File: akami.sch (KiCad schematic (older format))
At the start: 66 parts, among them J1 USB_C_Receptacle_USB2.0, J2 Conn_01x01, J3 Conn_01x01, Q1 DMP21D0UT, Q2 DMP21D0UT, Q3 DMP21D0UT, U1 nRF52840, U2 TP4054, U3 LP5912-3.3DRV, U4 ProMicro_2, Y1 32MHz, Y2 32.768 kHz

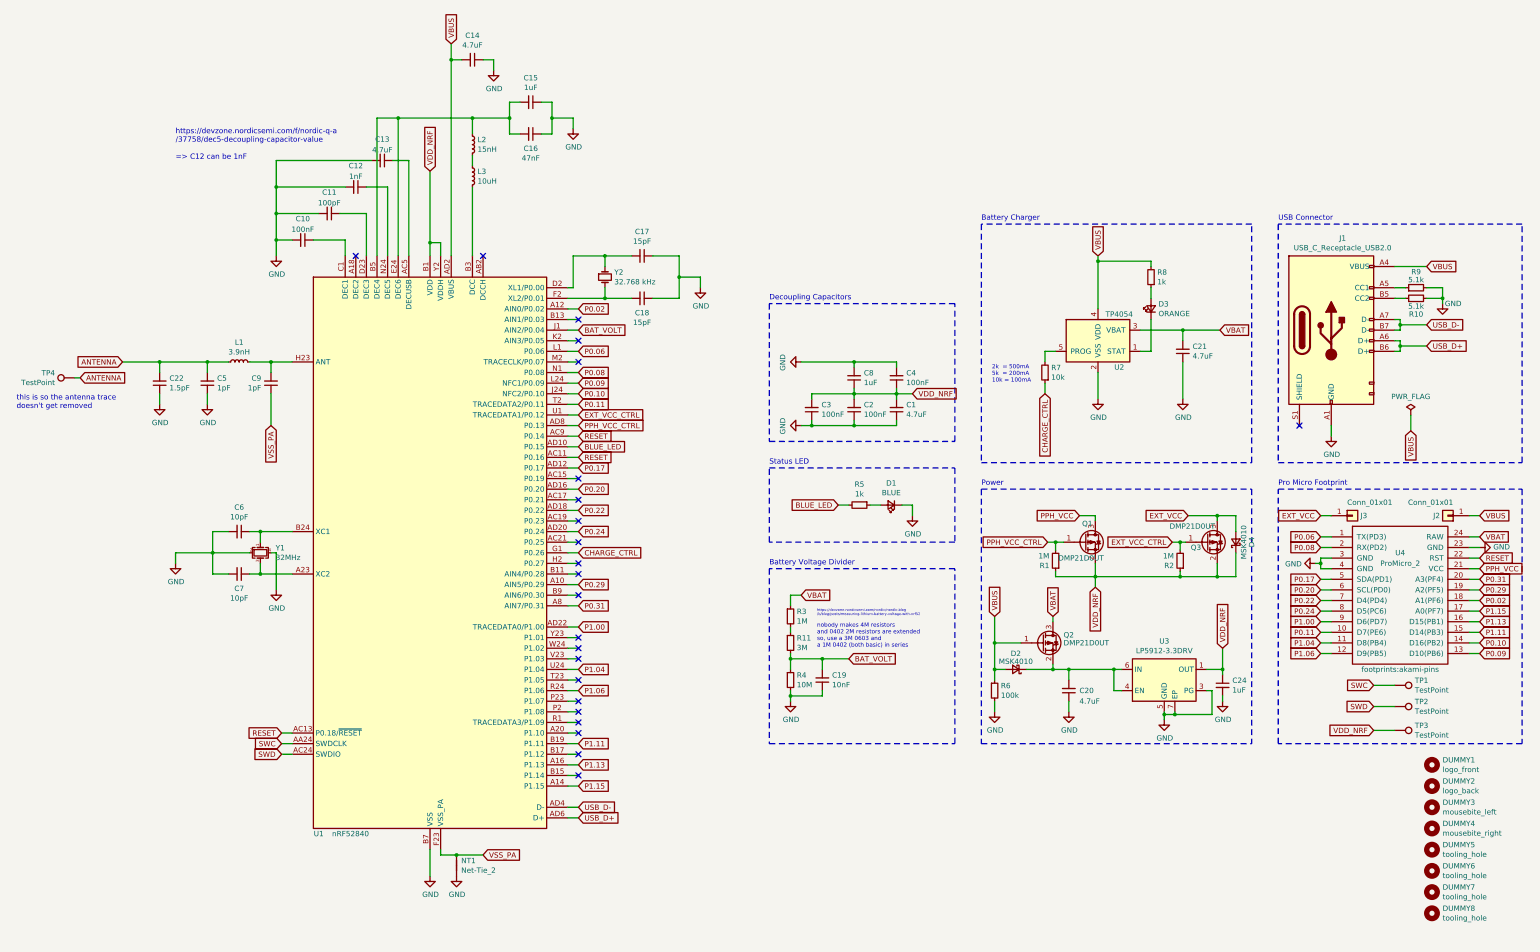
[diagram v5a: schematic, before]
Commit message: rev 3.2
1. re-layout and re-route the entire thing
2. as part of (1), move the nrf chip up by 0.75mm
3. add a 1uF capacitor on the VBUS input to the charger IC
4. move components further away from the USB connector since that
   has to be hand-soldered
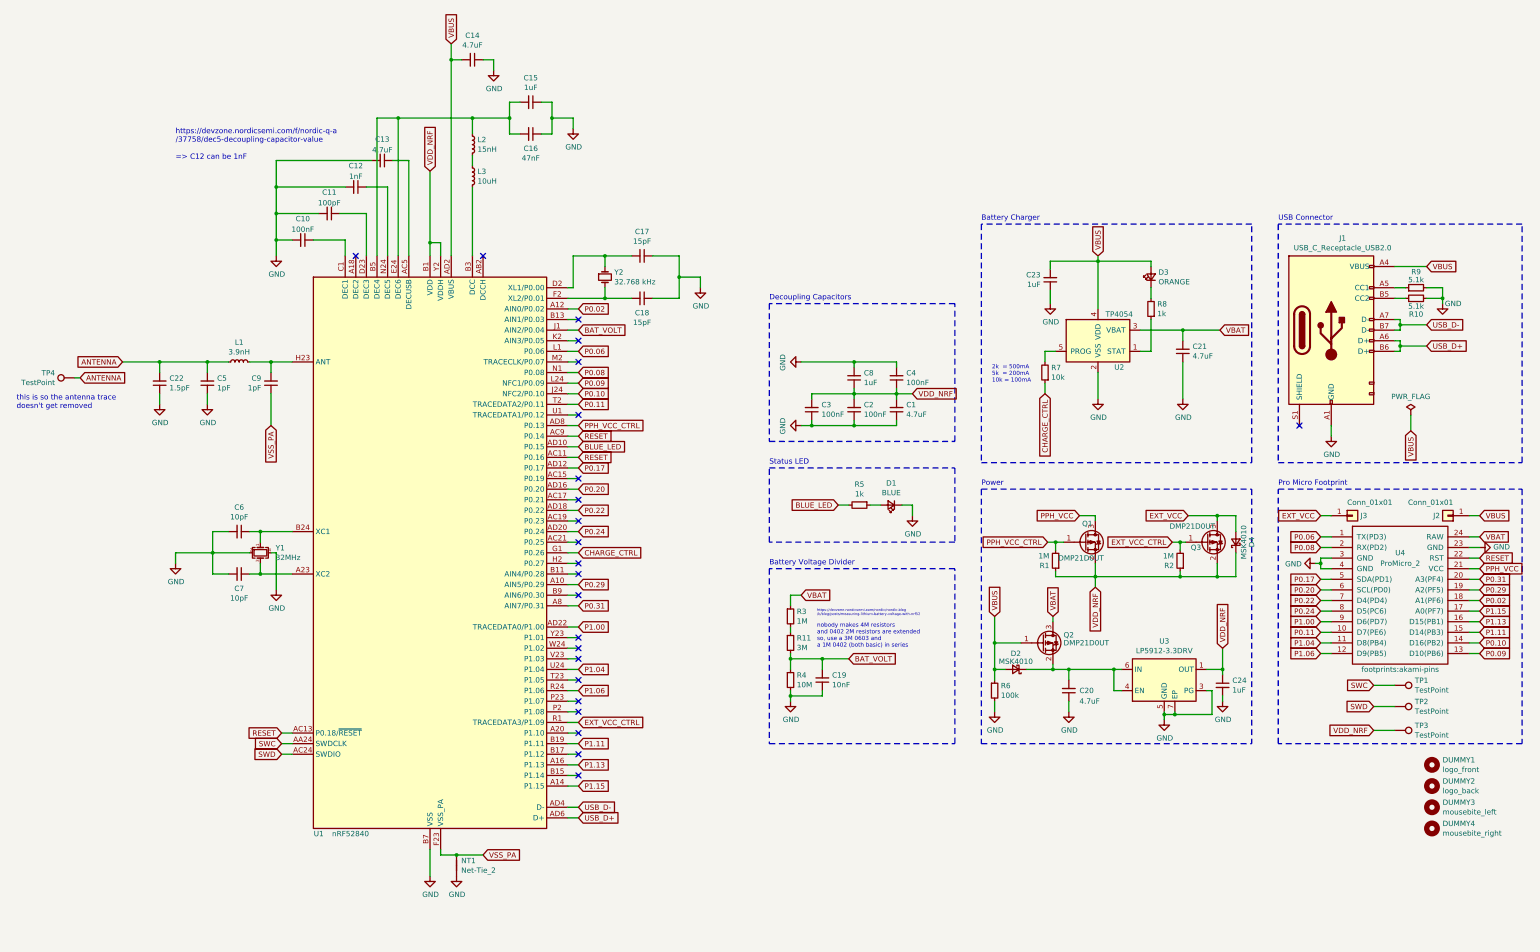
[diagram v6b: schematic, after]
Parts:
- removed DUMMY5, DUMMY6, DUMMY7, DUMMY8: tooling_hole, footprints:jlcpcb_tooling_hole, symbol Mechanical:MountingHole
- added C23: 1uF, Capacitor_SMD:C_0402_1005Metric, symbol Device:C_Small
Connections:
- net EXT_VCC_CTRL: now also U1.R1 (TRACEDATA3/P1.09); no longer U1.U1 (TRACEDATA1/P0.12)
- net GND: now also C23.1
- net VBUS: now also D3.2 (A), C23.2; no longer R8.2
- net at U2.1 (STAT): now also R8.1; no longer D3.1 (K)
- new net: D3.1 (K), R8.2
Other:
- moved on the sheet: D3, R8
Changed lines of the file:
@@
-$EndComp
-$Comp
-L Device:C_Small C8
-U 1 1 5FEB5801
-P 9200 4300
-F 0 "C8" H 9108 4254 50  0000 R CNN
-F 1 "1uF" H 9108 4345 50  0000 R CNN
-F 2 "Capacitor_SMD:C_0402_1005Metric" H 9200 4300 50  0001 C CNN
-F 3 "~" H 9200 4300 50  0001 C CNN
-F 4 "C52923" H 9200 4300 50  0001 C CNN "LCSC Part"
-	1    9200 4300
-	-1   0    0    1
 $EndComp
 $Comp
@@
 L Device:LED_Small D3
 U 1 1 5FFAD26F
-P 12000 3650
-F 0 "D3" V 12046 3580 50  0000 R CNN
-F 1 "ORANGE" V 11955 3580 50  0000 R CNN
-F 2 "LED_SMD:LED_0603_1608Metric" V 12000 3650 50  0001 C CNN
-F 3 "~" V 12000 3650 50  0001 C CNN
-F 4 "C2286" H 12000 3650 50  0001 C CNN "LCSC Part"
-	1    12000 3650
+P 12000 3350
+F 0 "D3" V 12046 3280 50  0000 R CNN
+F 1 "ORANGE" V 11955 3280 50  0000 R CNN
+F 2 "LED_SMD:LED_0603_1608Metric" V 12000 3350 50  0001 C CNN
+F 3 "~" V 12000 3350 50  0001 C CNN
+F 4 "C2286" H 12000 3350 50  0001 C CNN "LCSC Part"
+	1    12000 3350
 	0    -1   -1   0
 $EndComp
@@
 L Device:R_Small R8
 U 1 1 5FFBCDAA
-P 12000 3350
-F 0 "R8" H 11941 3304 50  0000 R CNN
-F 1 "1k" H 11941 3395 50  0000 R CNN
-F 2 "Resistor_SMD:R_0402_1005Metric" H 12000 3350 50  0001 C CNN
-F 3 "~" H 12000 3350 50  0001 C CNN
-F 4 "C11702" H 12000 3350 50  0001 C CNN "LCSC Part"
-	1    12000 3350
+P 12000 3650
+F 0 "R8" H 11941 3604 50  0000 R CNN
+F 1 "1k" H 11941 3695 50  0000 R CNN
+F 2 "Resistor_SMD:R_0402_1005Metric" H 12000 3650 50  0001 C CNN
+F 3 "~" H 12000 3650 50  0001 C CNN
+F 4 "C11702" H 12000 3650 50  0001 C CNN "LCSC Part"
+	1    12000 3650
 	-1   0    0    1
 $EndComp
@@
 NoConn ~ 6600 7350
 NoConn ~ 6600 7450
-NoConn ~ 6600 7550
 NoConn ~ 6600 7850
 NoConn ~ 6600 8050
@@
 $EndComp
 $Comp
-L Mechanical:MountingHole DUMMY5
-U 1 1 60BBBC37
-P 14650 8750
-F 0 "DUMMY5" H 14750 8796 50  0000 L CNN
-F 1 "tooling_hole" H 14750 8705 50  0000 L CNN
-F 2 "footprints:jlcpcb_tooling_hole" H 14650 8750 50  0001 C CNN
-F 3 "~" H 14650 8750 50  0001 C CNN
-	1    14650 8750
-	1    0    0    -1
-$EndComp
-$Comp
-L Mechanical:MountingHole DUMMY6
-U 1 1 60BBDE3A
-P 14650 8950
-F 0 "DUMMY6" H 14750 8996 50  0000 L CNN
-F 1 "tooling_hole" H 14750 8905 50  0000 L CNN
-F 2 "footprints:jlcpcb_tooling_hole" H 14650 8950 50  0001 C CNN
-F 3 "~" H 14650 8950 50  0001 C CNN
-	1    14650 8950
-	1    0    0    -1
-$EndComp
-$Comp
-L Mechanical:MountingHole DUMMY8
-U 1 1 60BBE1CE
-P 14650 9350
-F 0 "DUMMY8" H 14750 9396 50  0000 L CNN
-F 1 "tooling_hole" H 14750 9305 50  0000 L CNN
-F 2 "footprints:jlcpcb_tooling_hole" H 14650 9350 50  0001 C CNN
-F 3 "~" H 14650 9350 50  0001 C CNN
-	1    14650 9350
-	1    0    0    -1
-$EndComp
-$Comp
-L Mechanical:MountingHole DUMMY7
-U 1 1 60BBE5E3
-P 14650 9150
-F 0 "DUMMY7" H 14750 9196 50  0000 L CNN
-F 1 "tooling_hole" H 14750 9105 50  0000 L CNN
-F 2 "footprints:jlcpcb_tooling_hole" H 14650 9150 50  0001 C CNN
-F 3 "~" H 14650 9150 50  0001 C CNN
-	1    14650 9150
-	1    0    0    -1
-$EndComp
-$Comp
 L Connector_Generic:Conn_01x01 J3
 U 1 1 6009CB51
@@
 Wire Wire Line
 	6600 4650 6500 4650
-Text GLabel 6600 4650 2    50   Input ~ 0
+Text GLabel 6600 7550 2    50   Input ~ 0
 EXT_VCC_CTRL
 NoConn ~ 6600 7650
@@
 	1    0    0    -1
 $EndComp
+NoConn ~ 6600 4650
+$Comp
+L Device:C_Small C8
+U 1 1 5FEB5801
+P 9200 4300
+F 0 "C8" H 9108 4254 50  0000 R CNN
+F 1 "1uF" H 9108 4345 50  0000 R CNN
+F 2 "Capacitor_SMD:C_0402_1005Metric" H 9200 4300 50  0001 C CNN
+F 3 "~" H 9200 4300 50  0001 C CNN
+F 4 "C52923" H 9200 4300 50  0001 C CNN "LCSC Part"
+	1    9200 4300
+	-1   0    0    1
+$EndComp
+$Comp
+L Device:C_Small C23
+U 1 1 6025FBAA
+P 11050 3375
+F 0 "C23" H 11142 3329 50  0000 L CNN
+F 1 "1uF" H 11142 3420 50  0000 L CNN
+F 2 "Capacitor_SMD:C_0402_1005Metric" H 11050 3375 50  0001 C CNN
+F 3 "~" H 11050 3375 50  0001 C CNN
+F 4 "C52923" H 11050 3375 50  0001 C CNN "LCSC Part"
+	1    11050 3375
+	-1   0    0    1
+$EndComp
+$Comp
+L power:GND #PWR02
+U 1 1 60276B08
+P 11050 3600
+F 0 "#PWR02" H 11050 3350 50  0001 C CNN
+F 1 "GND" H 11055 3427 50  0000 C CNN
+F 2 "" H 11050 3600 50  0001 C CNN
+F 3 "" H 11050 3600 50  0001 C CNN
+	1    11050 3600
+	1    0    0    -1
+$EndComp
+Wire Wire Line
+	11050 3200 11050 3275
+Wire Wire Line
+	11050 3200 11500 3200
+Wire Wire Line
+	11050 3475 11050 3600
 $EndSCHEMATC
